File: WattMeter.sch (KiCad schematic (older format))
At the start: 1 part

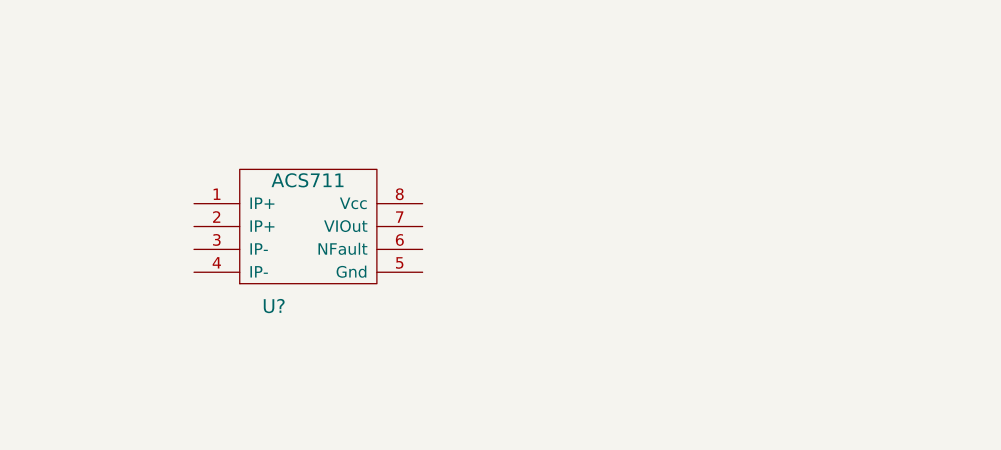
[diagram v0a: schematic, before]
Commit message: Add current amp
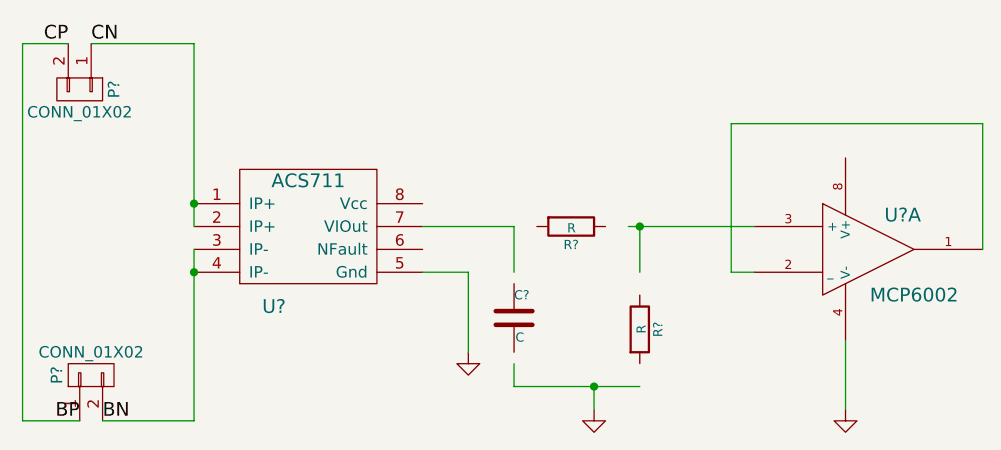
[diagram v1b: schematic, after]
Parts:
- added C?: C, symbol C
- added P? (x2): CONN_01X02, symbol CONN_01X02
- added R? (x2): R, symbol R
- added U?: MCP6002, symbol MCP6002
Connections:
- net labels added: BN, BP, CN, CP, GND
- wire segments 0 -> 21
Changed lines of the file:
@@
 	1    0    0    -1
 $EndComp
+$Comp
+L MCP6002 U?
+U 1 1 5512847B
+P 6050 2700
+F 0 "U?" H 6200 2850 60  0000 C CNN
+F 1 "MCP6002" H 6250 2500 60  0000 C CNN
+F 2 "" H 6050 2700 60  0000 C CNN
+F 3 "" H 6050 2700 60  0000 C CNN
+	1    6050 2700
+	1    0    0    -1
+$EndComp
+$Comp
+L GND #PWR?
+U 1 1 55128538
+P 4300 3150
+F 0 "#PWR?" H 4300 3150 30  0001 C CNN
+F 1 "GND" H 4300 3080 30  0001 C CNN
+F 2 "" H 4300 3150 60  0000 C CNN
+F 3 "" H 4300 3150 60  0000 C CNN
+	1    4300 3150
+	1    0    0    -1
+$EndComp
+Wire Wire Line
+	4300 2800 4300 3150
+Wire Wire Line
+	4100 2800 4300 2800
+$Comp
+L CONN_01X02 P?
+U 1 1 551290A7
+P 2650 3250
+F 0 "P?" H 2650 3400 50  0000 C CNN
+F 1 "CONN_01X02" V 2750 3250 50  0000 C CNN
+F 2 "" H 2650 3250 60  0000 C CNN
+F 3 "" H 2650 3250 60  0000 C CNN
+	1    2650 3250
+	0    -1   -1   0
+$EndComp
+$Comp
+L CONN_01X02 P?
+U 1 1 551290F8
+P 2600 2000
+F 0 "P?" H 2600 2150 50  0000 C CNN
+F 1 "CONN_01X02" V 2700 2000 50  0000 C CNN
+F 2 "" H 2600 2000 60  0000 C CNN
+F 3 "" H 2600 2000 60  0000 C CNN
+	1    2600 2000
+	0    1    1    0
+$EndComp
+Text Label 2700 3450 0    60   ~ 0
+BN
+Text Label 2600 3450 2    60   ~ 0
+BP
+Text Label 2650 1800 0    60   ~ 0
+CN
+Text Label 2550 1800 2    60   ~ 0
+CP
+Wire Wire Line
+	2600 3450 2350 3450
+Wire Wire Line
+	2350 3450 2350 1800
+Wire Wire Line
+	2350 1800 2550 1800
+Wire Wire Line
+	3100 3450 2700 3450
+Wire Wire Line
+	3100 2700 3100 3450
+Connection ~ 3100 2800
+Wire Wire Line
+	3100 1800 3100 2600
+Wire Wire Line
+	3100 1800 2650 1800
+Connection ~ 3100 2500
+$Comp
+L R R?
+U 1 1 5512B460
+P 4750 2600
+F 0 "R?" V 4830 2600 40  0000 C CNN
+F 1 "R" V 4757 2601 40  0000 C CNN
+F 2 "" V 4680 2600 30  0000 C CNN
+F 3 "" H 4750 2600 30  0000 C CNN
+	1    4750 2600
+	0    1    1    0
+$EndComp
+$Comp
+L R R?
+U 1 1 5512B4CB
+P 5050 3050
+F 0 "R?" V 5130 3050 40  0000 C CNN
+F 1 "R" V 5057 3051 40  0000 C CNN
+F 2 "" V 4980 3050 30  0000 C CNN
+F 3 "" H 5050 3050 30  0000 C CNN
+	1    5050 3050
+	1    0    0    -1
+$EndComp
+$Comp
+L C C?
+U 1 1 5512B53C
+P 4500 3000
+F 0 "C?" H 4500 3100 40  0000 L CNN
+F 1 "C" H 4506 2915 40  0000 L CNN
+F 2 "" H 4538 2850 30  0000 C CNN
+F 3 "" H 4500 3000 60  0000 C CNN
+	1    4500 3000
+	1    0    0    -1
+$EndComp
+$Comp
+L GND #PWR?
+U 1 1 5512B60A
+P 4850 3400
+F 0 "#PWR?" H 4850 3400 30  0001 C CNN
+F 1 "GND" H 4850 3330 30  0001 C CNN
+F 2 "" H 4850 3400 60  0000 C CNN
+F 3 "" H 4850 3400 60  0000 C CNN
+	1    4850 3400
+	1    0    0    -1
+$EndComp
+Wire Wire Line
+	4500 3200 4500 3300
+Wire Wire Line
+	4500 3300 5050 3300
+Wire Wire Line
+	4850 3300 4850 3400
+Connection ~ 4850 3300
+Wire Wire Line
+	4100 2600 4500 2600
+Wire Wire Line
+	4500 2600 4500 2800
+Wire Wire Line
+	5050 2800 5050 2600
+Connection ~ 5050 2600
+Wire Wire Line
+	5000 2600 5550 2600
+$Comp
+L GND #PWR?
+U 1 1 5512B926
+P 5950 3400
+F 0 "#PWR?" H 5950 3400 30  0001 C CNN
+F 1 "GND" H 5950 3330 30  0001 C CNN
+F 2 "" H 5950 3400 60  0000 C CNN
+F 3 "" H 5950 3400 60  0000 C CNN
+	1    5950 3400
+	1    0    0    -1
+$EndComp
+Wire Wire Line
+	5950 3400 5950 3100
+Wire Wire Line
+	6550 2700 6550 2150
+Wire Wire Line
+	6550 2150 5450 2150
+Wire Wire Line
+	5450 2150 5450 2800
+Wire Wire Line
+	5450 2800 5550 2800
 $EndSCHEMATC

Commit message: Add filter
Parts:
- C1: renamed from C?; value C -> 6u8
- R1: renamed from R?; value R -> 3.3k
- R2: renamed from R?; value R -> 6.7K
- gave numbers to parts that had none: 4
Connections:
- wire segments 21 -> 22
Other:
- note added: "Add filter and use 2nd half of op amp for battery measure.\nAdd on board temp sensor\nAdd off board temp sensor\nExternal serial for gps, display, (comms to pc?)\nAdd SD card socket"
- note added: "Add jumpers to select power from convertor or mbed and disconnect mbed even if using on board"
- moved on the sheet: C1
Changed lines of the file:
@@
 $EndDescr
 $Comp
-L ACS711 U?
+L ACS711 U1
 U 1 1 5511C6C0
 P 3650 2650
-F 0 "U?" H 3450 2350 60  0000 C CNN
+F 0 "U1" H 3450 2350 60  0000 C CNN
 F 1 "ACS711" H 3600 2900 60  0000 C CNN
 F 2 "" H 3650 2650 60  0000 C CNN
@@
 $EndComp
 $Comp
-L MCP6002 U?
+L MCP6002 U2
 U 1 1 5512847B
 P 6050 2700
-F 0 "U?" H 6200 2850 60  0000 C CNN
+F 0 "U2" H 6200 2850 60  0000 C CNN
 F 1 "MCP6002" H 6250 2500 60  0000 C CNN
 F 2 "" H 6050 2700 60  0000 C CNN
@@
 $EndComp
 $Comp
-L GND #PWR?
+L GND #PWR1
 U 1 1 55128538
 P 4300 3150
-F 0 "#PWR?" H 4300 3150 30  0001 C CNN
+F 0 "#PWR1" H 4300 3150 30  0001 C CNN
 F 1 "GND" H 4300 3080 30  0001 C CNN
 F 2 "" H 4300 3150 60  0000 C CNN
@@
 	4100 2800 4300 2800
 $Comp
-L CONN_01X02 P?
+L CONN_01X02 P2
 U 1 1 551290A7
 P 2650 3250
-F 0 "P?" H 2650 3400 50  0000 C CNN
+F 0 "P2" H 2650 3400 50  0000 C CNN
 F 1 "CONN_01X02" V 2750 3250 50  0000 C CNN
 F 2 "" H 2650 3250 60  0000 C CNN
@@
 $EndComp
 $Comp
-L CONN_01X02 P?
+L CONN_01X02 P1
 U 1 1 551290F8
 P 2600 2000
-F 0 "P?" H 2600 2150 50  0000 C CNN
+F 0 "P1" H 2600 2150 50  0000 C CNN
 F 1 "CONN_01X02" V 2700 2000 50  0000 C CNN
 F 2 "" H 2600 2000 60  0000 C CNN
@@
 Connection ~ 3100 2500
 $Comp
-L R R?
+L R R1
 U 1 1 5512B460
 P 4750 2600
-F 0 "R?" V 4830 2600 40  0000 C CNN
-F 1 "R" V 4757 2601 40  0000 C CNN
+F 0 "R1" V 4830 2600 40  0000 C CNN
+F 1 "3.3k" V 4757 2601 40  0000 C CNN
 F 2 "" V 4680 2600 30  0000 C CNN
 F 3 "" H 4750 2600 30  0000 C CNN
@@
 $EndComp
 $Comp
-L R R?
+L R R2
 U 1 1 5512B4CB
 P 5050 3050
-F 0 "R?" V 5130 3050 40  0000 C CNN
-F 1 "R" V 5057 3051 40  0000 C CNN
+F 0 "R2" V 5130 3050 40  0000 C CNN
+F 1 "6.7K" V 5057 3051 40  0000 C CNN
 F 2 "" V 4980 3050 30  0000 C CNN
 F 3 "" H 5050 3050 30  0000 C CNN
@@
 $EndComp
 $Comp
-L C C?
+L C C1
 U 1 1 5512B53C
-P 4500 3000
-F 0 "C?" H 4500 3100 40  0000 L CNN
-F 1 "C" H 4506 2915 40  0000 L CNN
-F 2 "" H 4538 2850 30  0000 C CNN
-F 3 "" H 4500 3000 60  0000 C CNN
-	1    4500 3000
+P 5300 3050
+F 0 "C1" H 5300 3150 40  0000 L CNN
+F 1 "6u8" H 5306 2965 40  0000 L CNN
+F 2 "" H 5338 2900 30  0000 C CNN
+F 3 "" H 5300 3050 60  0000 C CNN
+	1    5300 3050
 	1    0    0    -1
 $EndComp
 $Comp
-L GND #PWR?
+L GND #PWR2
 U 1 1 5512B60A
-P 4850 3400
-F 0 "#PWR?" H 4850 3400 30  0001 C CNN
-F 1 "GND" H 4850 3330 30  0001 C CNN
-F 2 "" H 4850 3400 60  0000 C CNN
-F 3 "" H 4850 3400 60  0000 C CNN
-	1    4850 3400
+P 5200 3400
+F 0 "#PWR2" H 5200 3400 30  0001 C CNN
+F 1 "GND" H 5200 3330 30  0001 C CNN
+F 2 "" H 5200 3400 60  0000 C CNN
+F 3 "" H 5200 3400 60  0000 C CNN
+	1    5200 3400
 	1    0    0    -1
 $EndComp
 Wire Wire Line
-	4500 3200 4500 3300
-Wire Wire Line
-	4500 3300 5050 3300
-Wire Wire Line
-	4850 3300 4850 3400
-Connection ~ 4850 3300
-Wire Wire Line
 	4100 2600 4500 2600
-Wire Wire Line
-	4500 2600 4500 2800
 Wire Wire Line
 	5050 2800 5050 2600
@@
 	5000 2600 5550 2600
 $Comp
-L GND #PWR?
+L GND #PWR3
 U 1 1 5512B926
 P 5950 3400
-F 0 "#PWR?" H 5950 3400 30  0001 C CNN
+F 0 "#PWR3" H 5950 3400 30  0001 C CNN
 F 1 "GND" H 5950 3330 30  0001 C CNN
 F 2 "" H 5950 3400 60  0000 C CNN
@@
 Wire Wire Line
 	5450 2800 5550 2800
+Wire Wire Line
+	5300 2600 5300 2850
+Connection ~ 5300 2600
+Wire Wire Line
+	5300 3350 5300 3250
+Wire Wire Line
+	5050 3350 5300 3350
+Wire Wire Line
+	5200 3350 5200 3400
+Wire Wire Line
+	5050 3300 5050 3350
+Connection ~ 5200 3350
+Text Notes 3350 1750 0    60   ~ 0
+Add jumpers to select power from convertor or mbed and disconnect mbed even if using on board
+Text Notes 3350 3950 0    60   ~ 0
+Add filter and use 2nd half of op amp for battery measure.\nAdd on board temp sensor\nAdd off board temp sensor\nExternal serial for gps, display, (comms to pc?)\nAdd SD card socket
 $EndSCHEMATC

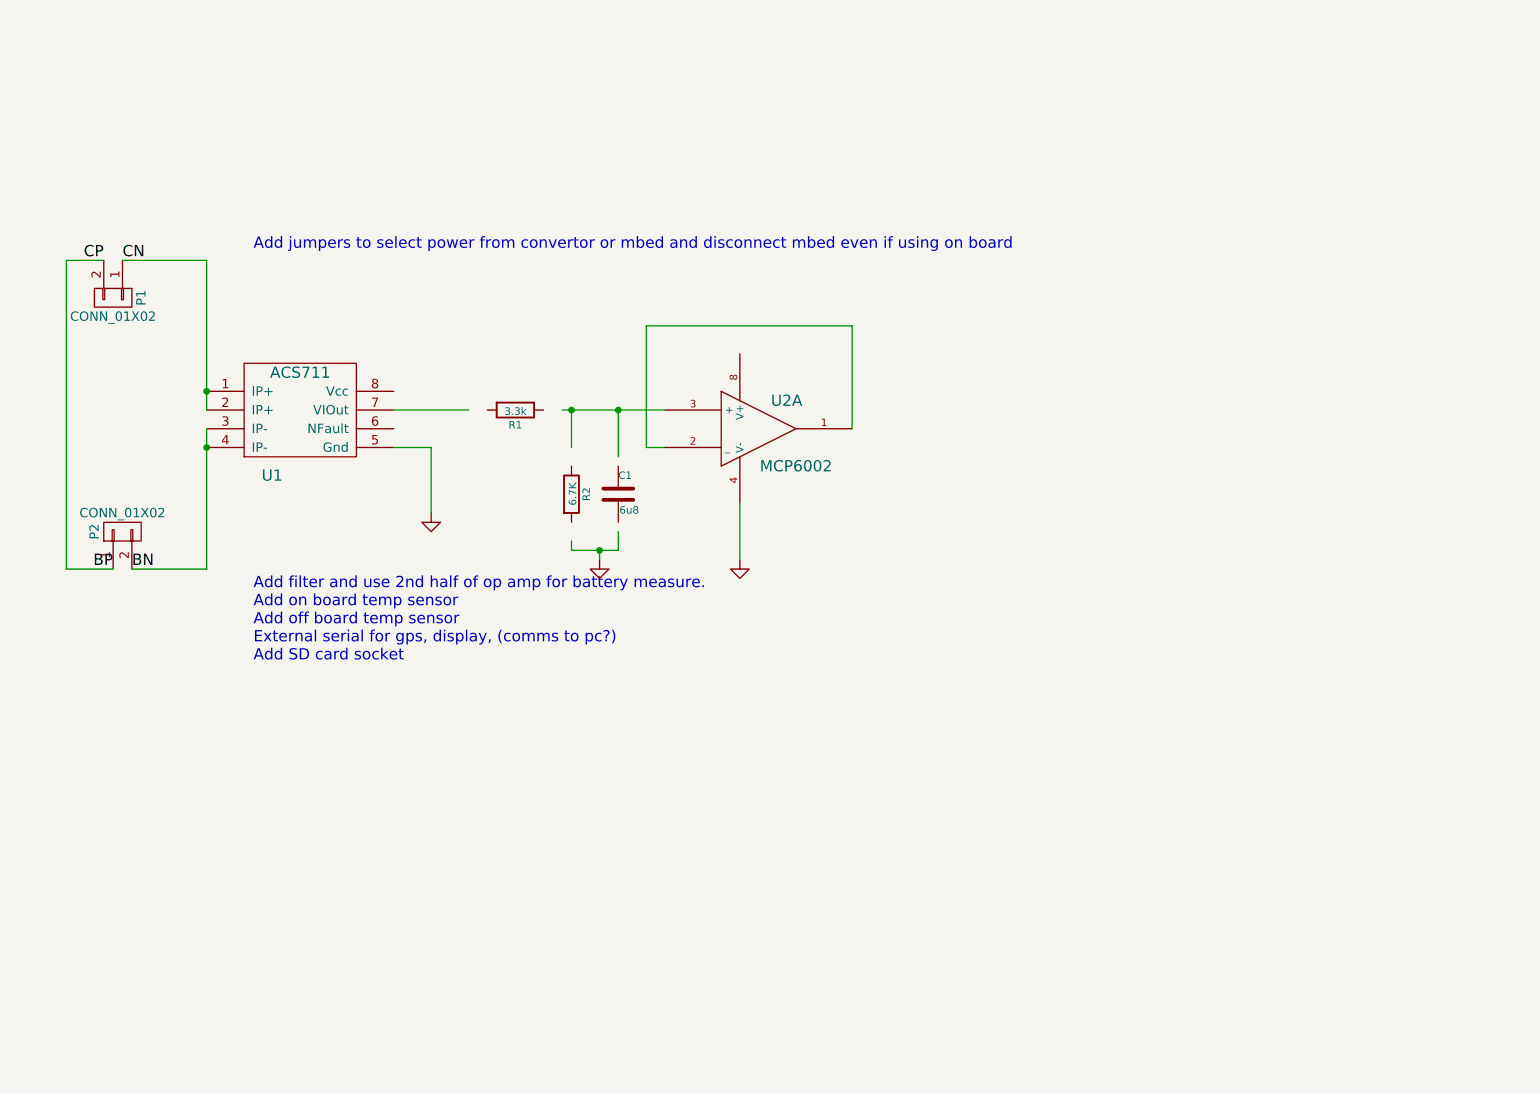
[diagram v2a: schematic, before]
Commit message: Voltage measure
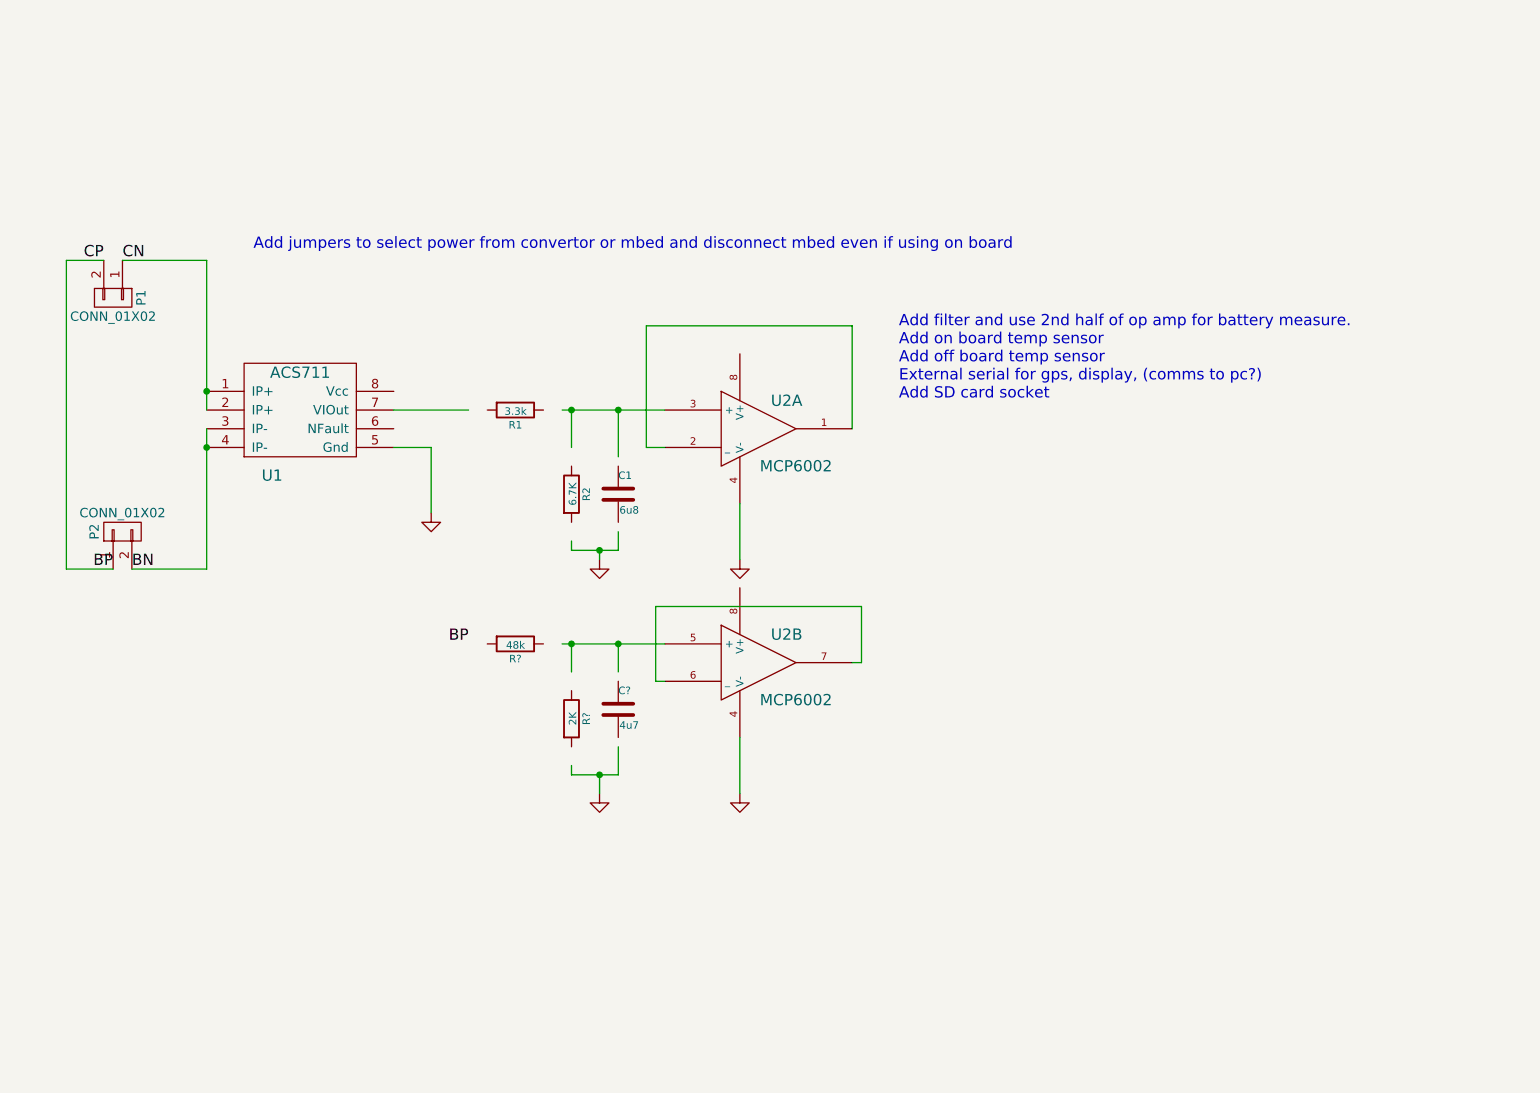
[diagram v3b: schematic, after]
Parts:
- added C?: 4u7, symbol C
- added R?: 48k, symbol R
- added R?: 2K, symbol R
- added unit 2 of U2
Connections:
- wire segments 22 -> 35
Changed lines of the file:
@@
 Text Notes 3350 1750 0    60   ~ 0
 Add jumpers to select power from convertor or mbed and disconnect mbed even if using on board
-Text Notes 3350 3950 0    60   ~ 0
+Text Notes 6800 2550 0    60   ~ 0
 Add filter and use 2nd half of op amp for battery measure.\nAdd on board temp sensor\nAdd off board temp sensor\nExternal serial for gps, display, (comms to pc?)\nAdd SD card socket
+$Comp
+L R R?
+U 1 1 5513D560
+P 4750 3850
+F 0 "R?" V 4830 3850 40  0000 C CNN
+F 1 "48k" V 4757 3851 40  0000 C CNN
+F 2 "" V 4680 3850 30  0000 C CNN
+F 3 "" H 4750 3850 30  0000 C CNN
+	1    4750 3850
+	0    1    1    0
+$EndComp
+$Comp
+L R R?
+U 1 1 5513D5D3
+P 5050 4250
+F 0 "R?" V 5130 4250 40  0000 C CNN
+F 1 "2K" V 5057 4251 40  0000 C CNN
+F 2 "" V 4980 4250 30  0000 C CNN
+F 3 "" H 5050 4250 30  0000 C CNN
+	1    5050 4250
+	1    0    0    -1
+$EndComp
+$Comp
+L C C?
+U 1 1 5513D606
+P 5300 4200
+F 0 "C?" H 5300 4300 40  0000 L CNN
+F 1 "4u7" H 5306 4115 40  0000 L CNN
+F 2 "" H 5338 4050 30  0000 C CNN
+F 3 "" H 5300 4200 60  0000 C CNN
+	1    5300 4200
+	1    0    0    -1
+$EndComp
+Text Label 4500 3850 2    60   ~ 0
+BP
+Wire Wire Line
+	5000 3850 5550 3850
+Wire Wire Line
+	5050 3850 5050 4000
+Wire Wire Line
+	5300 3850 5300 4000
+Connection ~ 5050 3850
+Wire Wire Line
+	5050 4500 5050 4550
+Wire Wire Line
+	5050 4550 5300 4550
+Wire Wire Line
+	5300 4550 5300 4400
+$Comp
+L GND #PWR?
+U 1 1 5513D6BA
+P 5200 4650
+F 0 "#PWR?" H 5200 4650 30  0001 C CNN
+F 1 "GND" H 5200 4580 30  0001 C CNN
+F 2 "" H 5200 4650 60  0000 C CNN
+F 3 "" H 5200 4650 60  0000 C CNN
+	1    5200 4650
+	1    0    0    -1
+$EndComp
+Wire Wire Line
+	5200 4650 5200 4550
+Connection ~ 5200 4550
+$Comp
+L MCP6002 U2
+U 2 1 5513D6FD
+P 6050 3950
+F 0 "U2" H 6200 4100 60  0000 C CNN
+F 1 "MCP6002" H 6250 3750 60  0000 C CNN
+F 2 "" H 6050 3950 60  0000 C CNN
+F 3 "" H 6050 3950 60  0000 C CNN
+	2    6050 3950
+	1    0    0    -1
+$EndComp
+Connection ~ 5300 3850
+Wire Wire Line
+	5550 4050 5500 4050
+Wire Wire Line
+	5500 4050 5500 3650
+Wire Wire Line
+	5500 3650 6600 3650
+Wire Wire Line
+	6600 3650 6600 3950
+Wire Wire Line
+	6600 3950 6550 3950
+$Comp
+L GND #PWR?
+U 1 1 5513D82C
+P 5950 4650
+F 0 "#PWR?" H 5950 4650 30  0001 C CNN
+F 1 "GND" H 5950 4580 30  0001 C CNN
+F 2 "" H 5950 4650 60  0000 C CNN
+F 3 "" H 5950 4650 60  0000 C CNN
+	1    5950 4650
+	1    0    0    -1
+$EndComp
+Wire Wire Line
+	5950 4350 5950 4650
 $EndSCHEMATC

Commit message: More work
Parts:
- added C1: 0.01uF, symbol C
- added C4: 47u, symbol C
- added D1: D_Schottky_Small, symbol D_Schottky_Small
- added JP1: Jumper_NC_Small, symbol Jumper_NC_Small
- added JP2: Jumper_NO_Small, symbol Jumper_NO_Small
- added L1: 68uF, symbol INDUCTOR_SMALL
- added P3: CONN_01X03, symbol CONN_01X03
- added P4, P5: CONN_01X04, symbol CONN_01X04
- added U1: LM2674, symbol LM2674
- added U4: MCP9700, symbol MCP9700
- gave numbers to parts that had none: 3
- renumbered C1 to C2, R2 to R3, U1 to U2, U2 to U3
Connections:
- net labels added: Rx1, Rx2, Tx1, Tx2, V33, Vmbed, Vsw
- wire segments 35 -> 57
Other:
- note added: "Add Connectors for Arduino/mbed"
